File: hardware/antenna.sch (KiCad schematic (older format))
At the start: 9 parts, among them P1 SATA

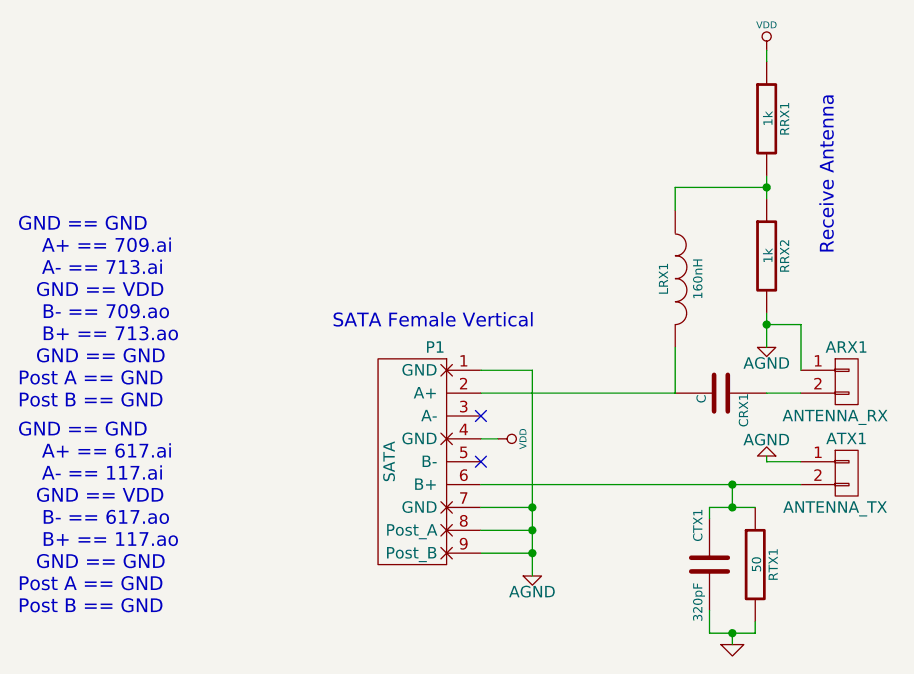
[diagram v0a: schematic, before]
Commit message: Use custom SATA connector for design-rule compatibility
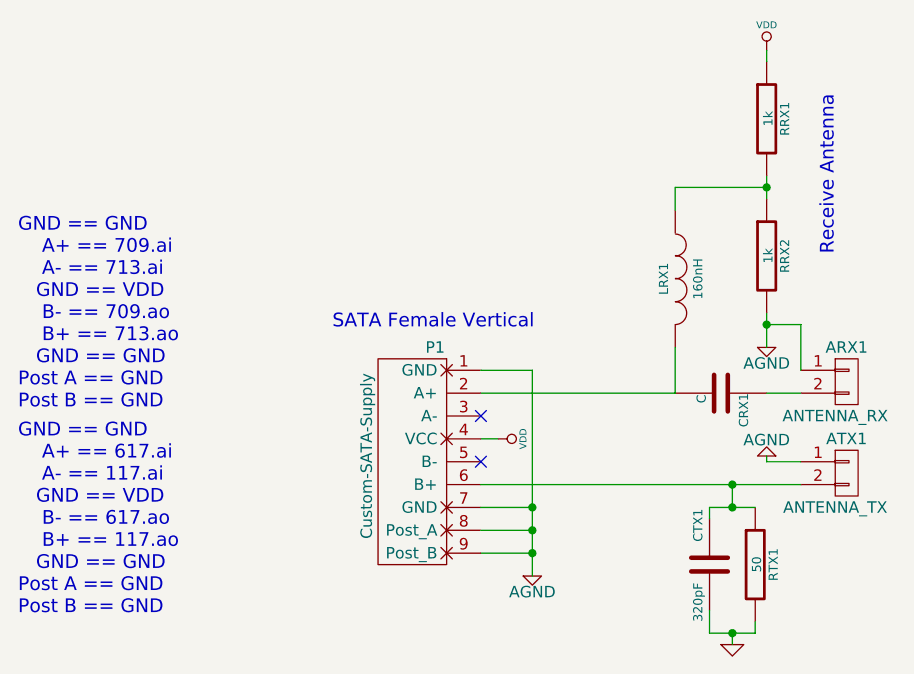
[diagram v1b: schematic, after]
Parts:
- removed P1: SATA, symbol SATA
- added P1: Custom-SATA-Supply, symbol Custom-SATA-Supply
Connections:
- net AGND: now also P1.1 (GND), P1.7 (GND), P1.8 (Post_A), P1.9 (Post_B)
- net VDD: now also P1.4 (VCC)
- net at CRX1.2, LRX1.2: now also P1.2 (A+)
- net at ATX1.2 (P2), CTX1.1, RTX1.1: now also P1.6 (B+)
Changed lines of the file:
@@
 	1    0    0    -1
 $EndComp
-$Comp
-L SATA P1
-U 1 1 54547579
-P 2725 2700
-F 0 "P1" H 2725 3200 50  0000 C CNN
-F 1 "SATA" V 2925 2700 50  0000 C CNN
-F 2 "" H 3075 2700 60  0000 C CNN
-F 3 "" H 3075 2700 60  0000 C CNN
-	1    2725 2700
-	-1   0    0    -1
-$EndComp
 Wire Wire Line
-	2925 2800 4325 2800
+	2925 2800 4025 2800
+Wire Wire Line
+	4025 2800 4325 2800
 Wire Wire Line
 	2925 2400 3775 2400
@@
 	3925 2900 3925 2950
 Wire Wire Line
-	3925 2900 4125 2900
+	3925 2900 4025 2900
+Wire Wire Line
+	4025 2900 4125 2900
 Connection ~ 4025 3450
 Wire Wire Line
@@
 	4025 3450 4025 3500
 Wire Wire Line
-	3925 3450 4125 3450
+	3925 3450 4025 3450
+Wire Wire Line
+	4025 3450 4125 3450
 Wire Wire Line
 	4125 3450 4125 3400
@@
 	4175 1500 3775 1500
 Wire Wire Line
-	4175 1450 4175 1550
+	4175 1450 4175 1500
 Wire Wire Line
-	4175 2050 4175 2200
+	4175 1500 4175 1550
+Wire Wire Line
+	4175 2050 4175 2100
+Wire Wire Line
+	4175 2100 4175 2200
 $Comp
 L AGND #PWR5
@@
 	2925 2300 3150 2300
 Wire Wire Line
-	3150 2300 3150 3200
+	3150 2300 3150 2900
+Wire Wire Line
+	3150 2900 3150 3000
+Wire Wire Line
+	3150 3000 3150 3100
+Wire Wire Line
+	3150 3100 3150 3200
 Wire Wire Line
 	2925 2900 3150 2900
@@
 Text Notes 2275 2125 0    60   ~ 0
 SATA Female Vertical
+$Comp
+L Custom-SATA-Supply P1
+U 1 1 5454D3DC
+P 2725 2700
+F 0 "P1" H 2725 3200 50  0000 C CNN
+F 1 "Custom-SATA-Supply" V 3025 2725 50  0000 C CNN
+F 2 "" H 3075 2700 60  0000 C CNN
+F 3 "" H 3075 2700 60  0000 C CNN
+	1    2725 2700
+	-1   0    0    -1
+$EndComp
 $EndSCHEMATC
